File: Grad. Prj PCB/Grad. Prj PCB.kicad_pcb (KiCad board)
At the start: 2 copper layers, 72 x 90 mm, 45 parts, among them J1 GPS, J2 Lock_4, J3 Lock_3, J4 Lock_2, J5 Lock_1, J6 POWER INPUT, J7 Pressure, J8 Heart Rate, J9 Vbatt, K1 POWER RELAY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

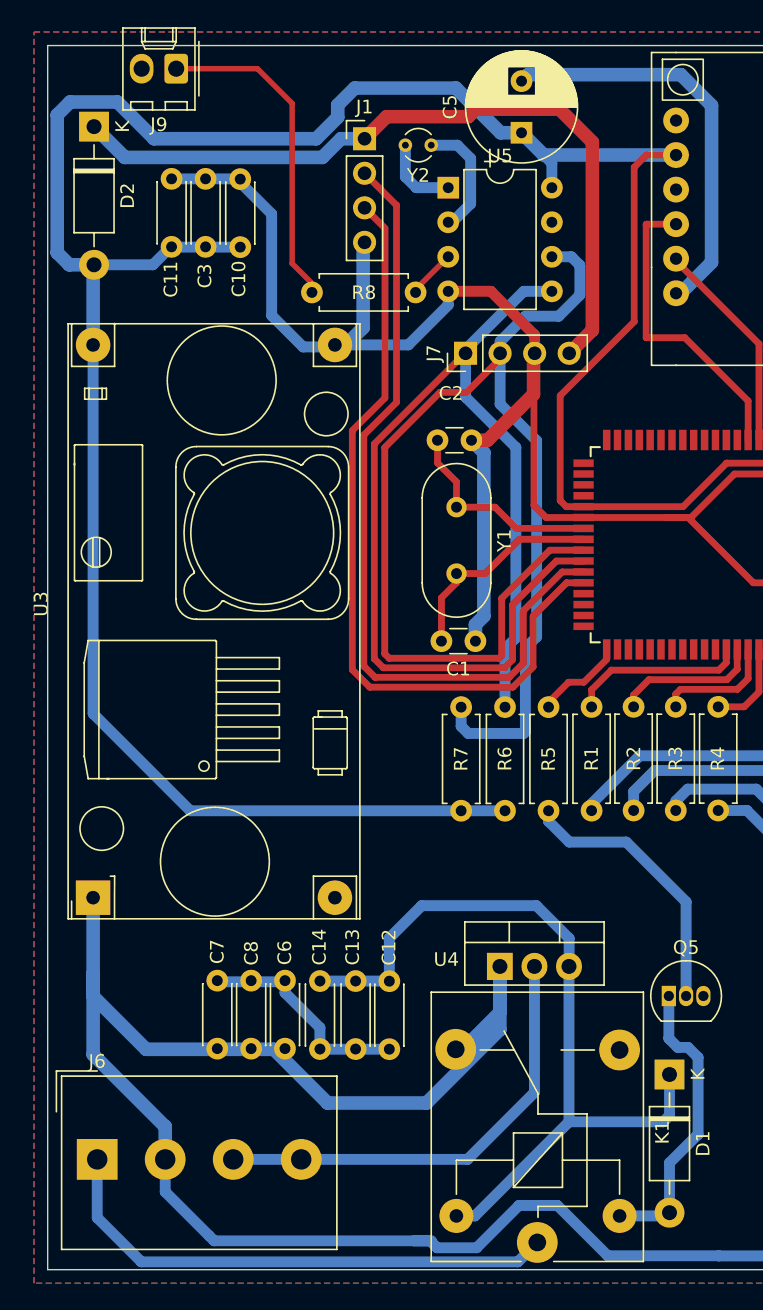
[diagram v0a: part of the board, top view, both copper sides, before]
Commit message: Added RTC
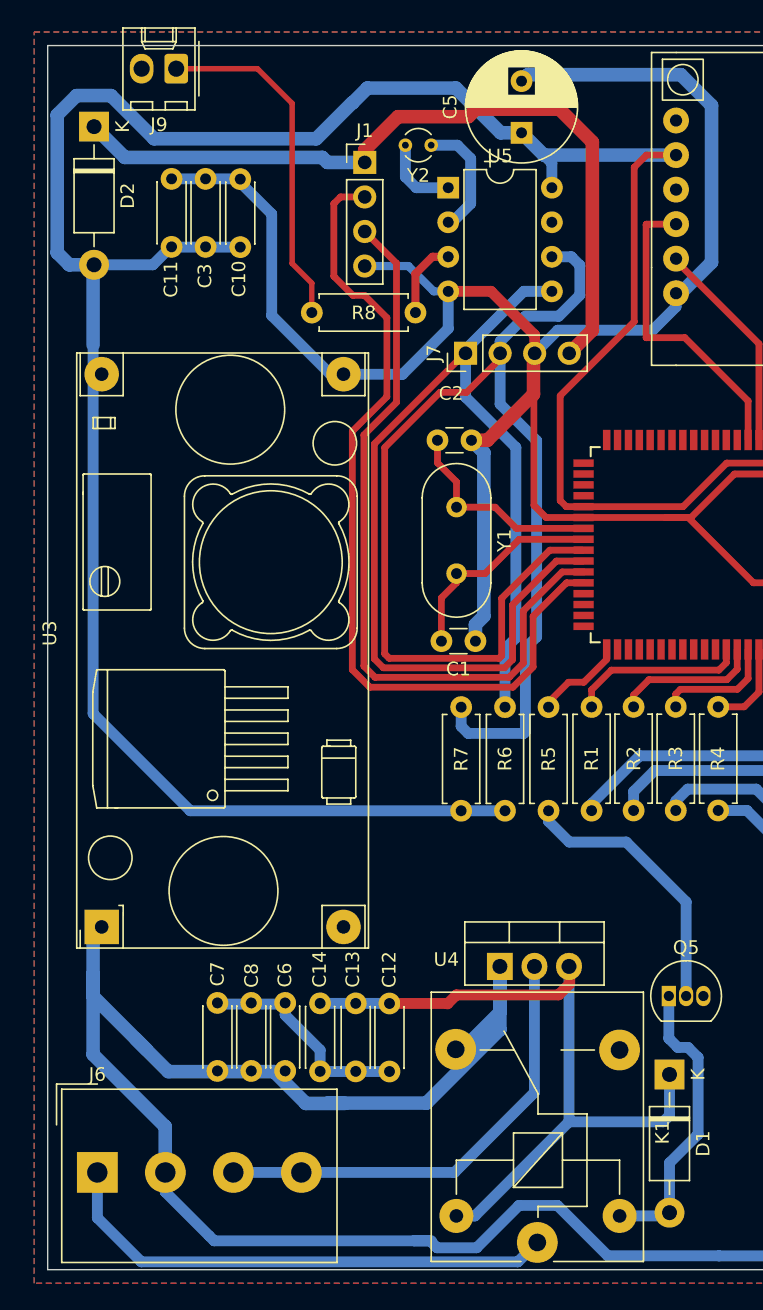
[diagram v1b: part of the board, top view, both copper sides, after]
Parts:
- moved U3 2.24 mm to (74.0, 104.8)
- moved J1 1.74 mm to (93.3, 48.6)
- moved C13 1.64 mm to (92.7, 110.4)
- moved C14 1.64 mm to (90.0, 110.4)
- moved C7 1.64 mm to (82.5, 115.4)
- moved C8 1.64 mm to (85.0, 115.4)
- moved C12 1.64 mm to (95.1, 110.4)
- moved C6 1.64 mm to (87.5, 115.4)
- moved R8 1.48 mm to (97.0, 59.6)
- moved J6 0.96 mm to (73.7, 122.9)
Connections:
- J1 pad 2: TX -> RX
- J1 pad 3: RX -> TX
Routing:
- net GND: track 221.1 -> 235.0 mm
- net +5V: track 58.7 -> 53.5 mm
- net RX: track 58.5 -> 62.8 mm
- net TX: track 60.2 -> 55.9 mm
- net Net-(R8-Pad1): track 4.04 -> 5.78 mm
- net Net-(J9-Pad1): track 24.1 -> 25.6 mm
- net 12vIN: track 38.6 -> 37.6 mm
- net +3.3V: track 56.3 -> 57.1 mm
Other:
- board text added: "+VBatt"
- board text added: "+VLine"
- board text added: "-VBatt"

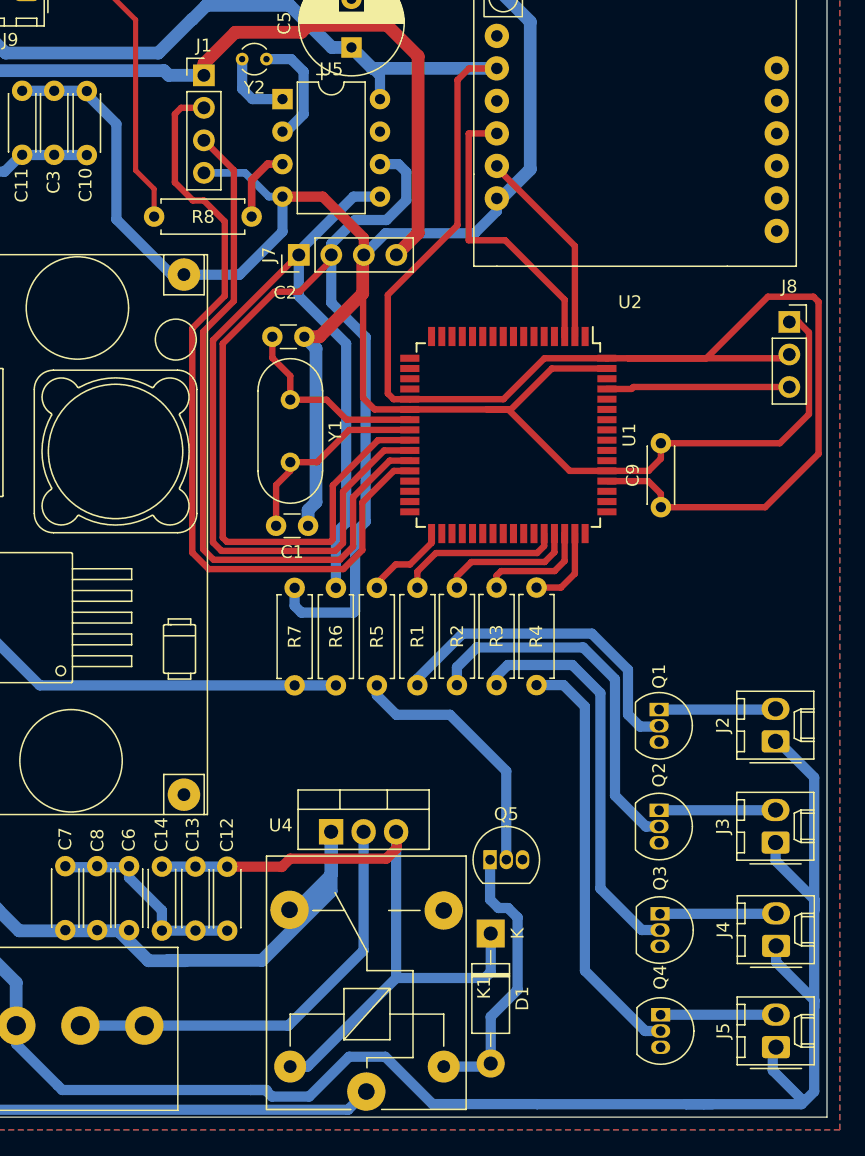
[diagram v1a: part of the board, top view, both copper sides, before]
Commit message: Added ISP Pin Header
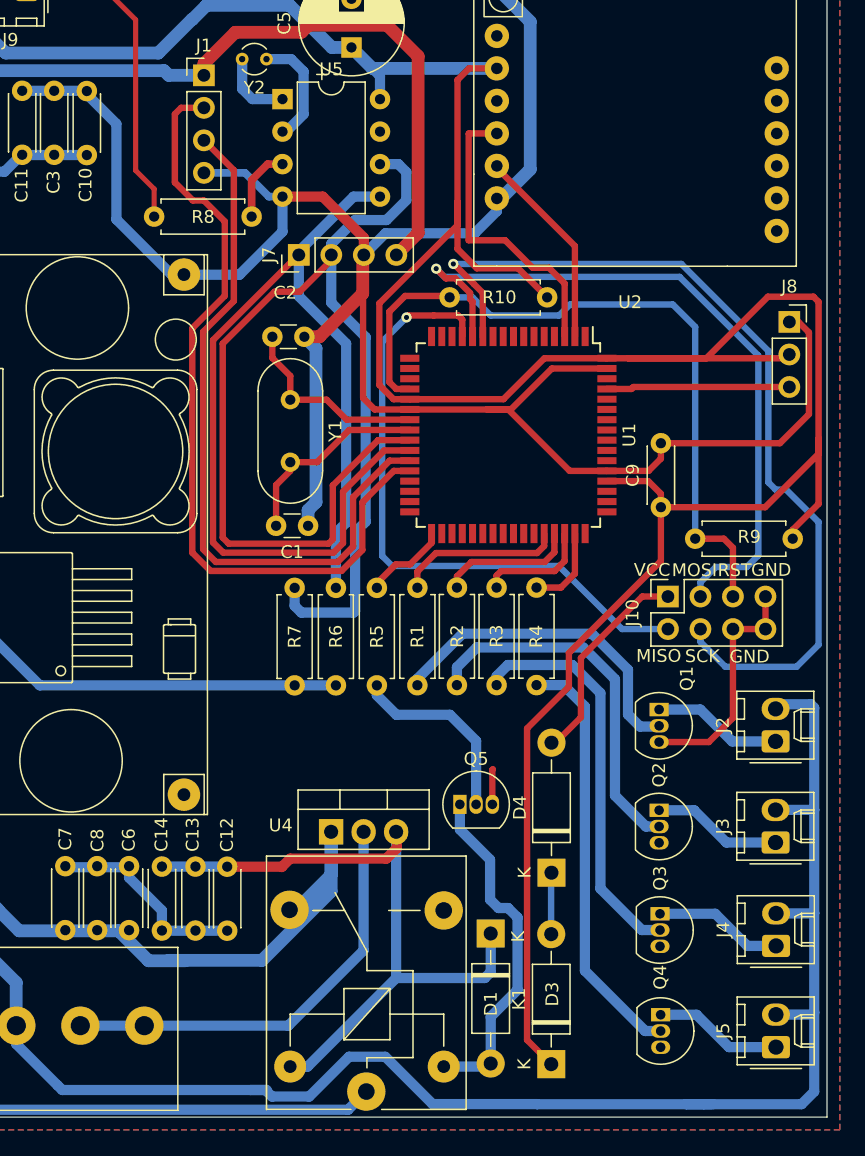
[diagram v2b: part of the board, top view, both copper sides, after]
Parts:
- added D3: 1N4007, Diode_THT:D_DO-41_SOD81_P10.16mm_Horizontal, F.Cu at (120.5, 125.9)
- added D4: 1N4007, Diode_THT:D_DO-41_SOD81_P10.16mm_Horizontal, F.Cu at (120.5, 110.9)
- added J10: ISP, Connector_PinSocket_2.54mm:PinSocket_2x04_P2.54mm_Vertical, F.Cu at (129.6, 89.3)
- added R10: 10K, Resistor_THT:R_Axial_DIN0207_L6.3mm_D2.5mm_P7.62mm_Horizontal, F.Cu at (112.5, 65.9)
- added R9: 10K, Resistor_THT:R_Axial_DIN0207_L6.3mm_D2.5mm_P7.62mm_Horizontal, F.Cu at (139.3, 84.8)
- moved Q5 4.92 mm to (113.3, 105.6)
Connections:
- J2 pad 1: 12vLine -> Lock_4
- J2 pad 2: Lock_4 -> 12vLine
- J3 pad 1: 12vLine -> Lock_3
- J3 pad 2: Lock_3 -> 12vLine
- J4 pad 1: 12vLine -> Lock_2
- J4 pad 2: Lock_2 -> 12vLine
- J5 pad 1: 12vLine -> Lock_1
- J5 pad 2: Lock_1 -> 12vLine
- U1 pad 11: unconnected-(U1-Pad11) -> SCK
- U1 pad 12: unconnected-(U1-Pad12) -> MOSI
- U1 pad 13: unconnected-(U1-Pad13) -> MISO
- U1 pad 20: unconnected-(U1-Pad20) -> RST
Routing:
- net SCK: track 0.00 -> 70.9 mm, vias 0 -> 1
- net +4V: track 258.6 -> 328.6 mm
- net RST: track 0.00 -> 57.1 mm
- net MOSI: track 0.00 -> 57.0 mm, vias 0 -> 1
- net MISO: track 0.00 -> 50.0 mm, vias 0 -> 1
- net GND: track 235.0 -> 256.4 mm
- net Net-(J10-Pad1): track 0.00 -> 16.6 mm
- net Net-(Q5-Pad2): track 20.3 -> 15.0 mm
- net Net-(D1-Pad2): track 21.9 -> 27.2 mm
- net Net-(D3-Pad2): track 0.00 -> 4.82 mm
- net 12vLine: track 191.9 -> 189.0 mm
- net Lock_4: track 9.12 -> 10.3 mm
- net Lock_1: track 9.01 -> 10.1 mm
- net Lock_3: track 9.11 -> 10.1 mm
- net Lock_2: track 9.08 -> 10.1 mm
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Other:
- board text added: "GND"
- board text added: "MISO"
- board text added: "MOSI"
- board text added: "RST"
- board text added: "SCK"
- board text added: "VCC"

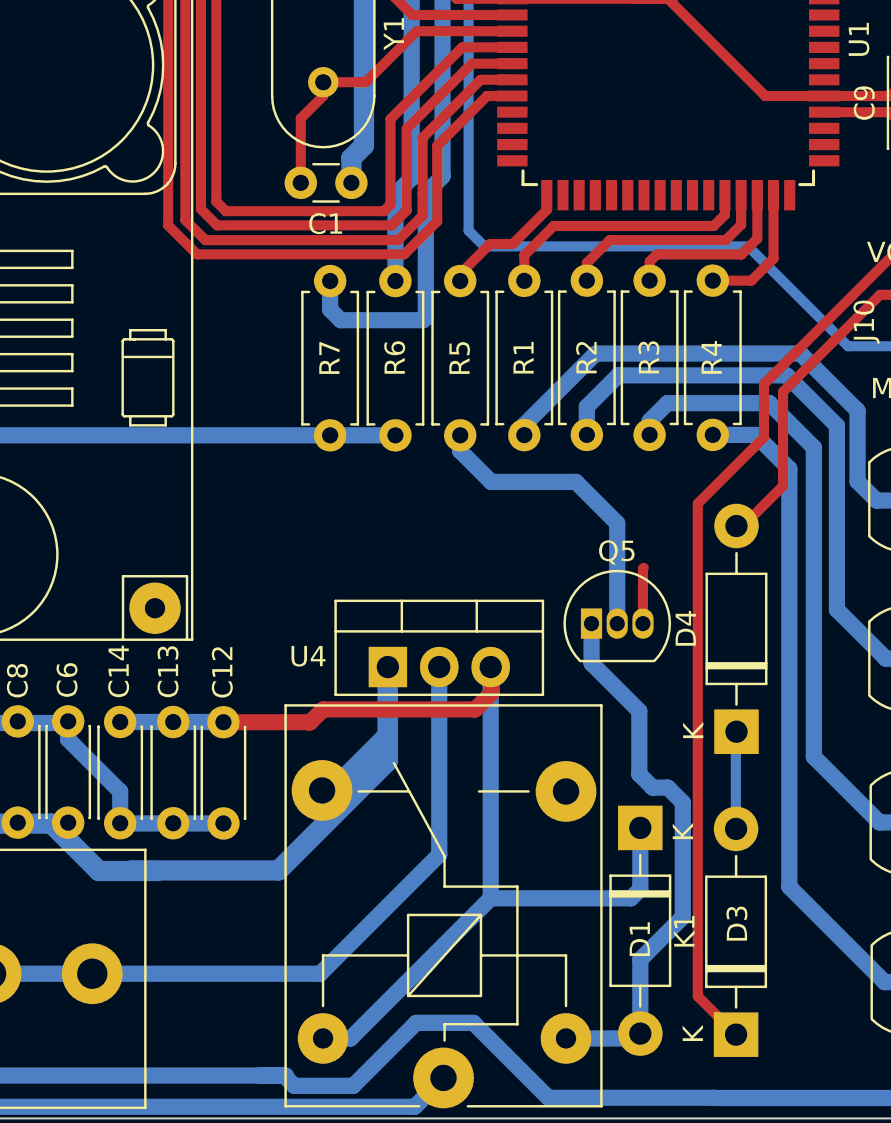
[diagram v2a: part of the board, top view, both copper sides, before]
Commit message: Added ISP Pin Header
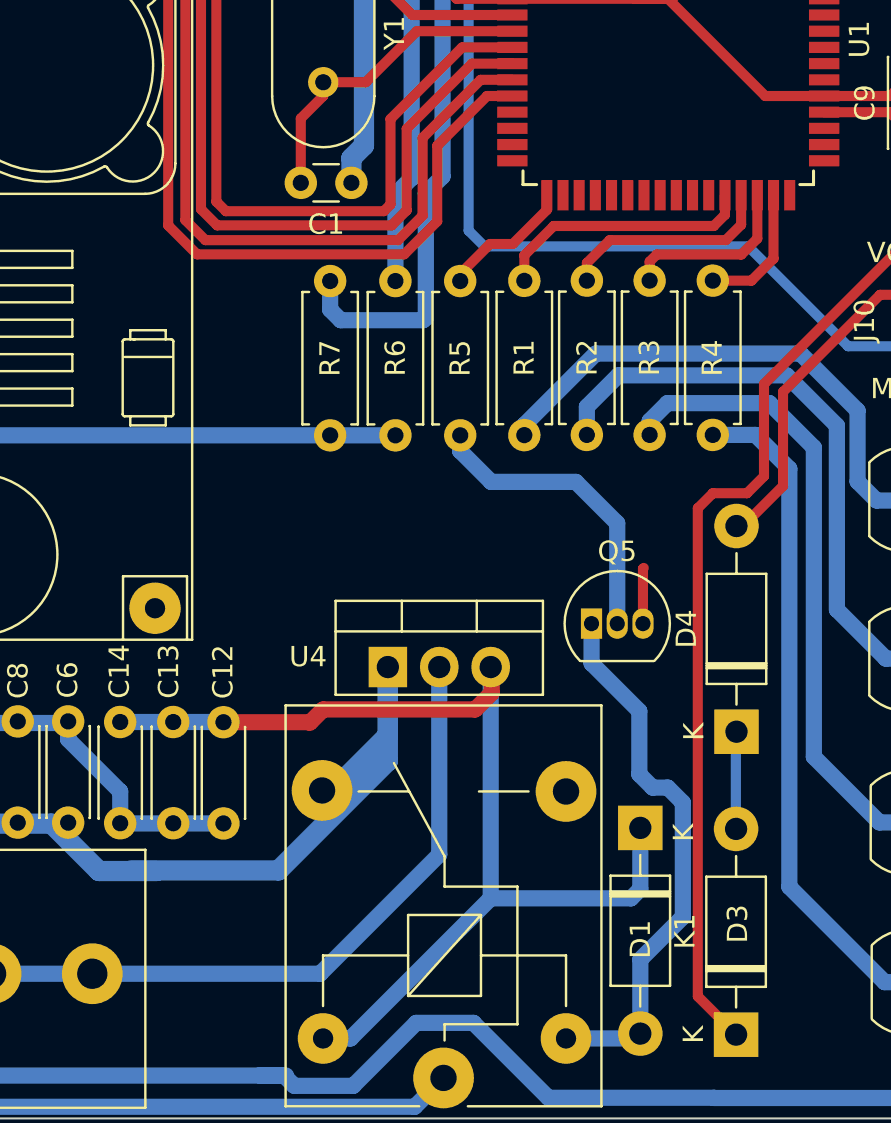
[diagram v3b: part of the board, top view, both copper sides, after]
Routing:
- net +4V: track 328.6 -> 329.6 mm
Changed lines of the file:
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@@
     (fp_arc (start 29.653011 17.437976) (mid 26.817397 18.185797) (end 23.981783 17.437976) (layer "F.SilkS") (width 0.12))
     (fp_arc (start 23.981784 7.433617) (mid 26.817398 6.685796) (end 29.653011 7.433617) (layer "F.SilkS") (width 0.12))
-    (fp_arc (start 23.847611 17.472062) (mid 23.907831 17.428018) (end 23.981783 17.437976) (layer "F.SilkS") (width 0.12))
-    (fp_arc (start 13.181636 16.183217) (mid 13.252317 16.21252) (end 13.281636 16.283217) (layer "F.SilkS") (width 0.12))
+    (fp_arc (start 23.847611 17.472062) (mid 23.907835 17.428062) (end 23.981783 17.437976) (layer "F.SilkS") (width 0.12))
+    (fp_arc (start 13.181636 16.183217) (mid 13.252353 16.212514) (end 13.281636 16.283217) (layer "F.SilkS") (width 0.12))
     (fp_arc (start 21.815217 15.271409) (mid 21.825126 15.345337) (end 21.781132 15.405582) (layer "F.SilkS") (width 0.12))
     (fp_arc (start 23.981783 7.433617) (mid 23.907854 7.443509) (end 23.847611 7.399531) (layer "F.SilkS") (width 0.12))
@@
     (fp_arc (start 31.853663 15.405583) (mid 31.809646 15.345344) (end 31.819576 15.27141) (layer "F.SilkS") (width 0.12))
     (fp_arc (start 33.299783 3.582294) (mid 33.285139 3.617647) (end 33.249783 3.632294) (layer "F.SilkS") (width 0.12))
-    (fp_arc (start 9.581636 18.683217) (mid 9.510896 18.653941) (end 9.481636 18.583217) (layer "F.SilkS") (width 0.12))
+    (fp_arc (start 9.581636 18.683217) (mid 9.510931 18.653935) (end 9.481636 18.583217) (layer "F.SilkS") (width 0.12))
     (fp_arc (start 21.815218 15.27141) (mid 21.067399 12.435797) (end 21.815218 9.600183) (layer "F.SilkS") (width 0.12))
     (fp_arc (start 21.781131 9.46601) (mid 21.825179 9.52623) (end 21.815218 9.600183) (layer "F.SilkS") (width 0.12))
@@
   (segment (start 98.66 69.02) (end 98.66 70.68) (width 0.5) (layer "F.Cu") (net 3))
   (segment (start 104.46 75.5) (end 102.9 73.94) (width 0.5) (layer "F.Cu") (net 3))
-  (segment (start 120.45 125.86) (end 118.56 123.97) (width 0.5) (layer "F.Cu") (net 4))
+  (segment (start 129.02 86.54) (end 129.02 82.34) (width 0.5) (layer "F.Cu") (net 4))
   (segment (start 141.34 82.08) (end 141.34 76.97) (width 0.5) (layer "F.Cu") (net 4))
   (segment (start 138.76 70.7) (end 139.055 70.405) (width 0.5) (layer "F.Cu") (net 4))
@@
   (segment (start 124.8 70.7) (end 126.46 70.7) (width 0.5) (layer "F.Cu") (net 4))
   (segment (start 126.46 70.7) (end 138.76 70.7) (width 0.5) (layer "F.Cu") (net 4))
+  (segment (start 119.3 99.12) (end 120.99 99.12) (width 0.5) (layer "F.Cu") (net 4))
   (segment (start 129.02 82.34) (end 137.17 82.34) (width 0.5) (layer "F.Cu") (net 4))
-  (segment (start 118.56 123.97) (end 118.56 99.63) (width 0.5) (layer "F.Cu") (net 4))
+  (segment (start 121.83 93.73) (end 129.02 86.54) (width 0.5) (layer "F.Cu") (net 4))
+  (segment (start 118.56 123.97) (end 118.56 99.86) (width 0.5) (layer "F.Cu") (net 4))
+  (segment (start 121.83 98.28) (end 121.83 93.73) (width 0.5) (layer "F.Cu") (net 4))
   (segment (start 141.34 76.97) (end 141.34 66.29) (width 0.5) (layer "F.Cu") (net 4))
   (segment (start 109.4 73.9) (end 116.72 73.9) (width 0.5) (layer "F.Cu") (net 4))
@@
   (segment (start 108.13 73.9) (end 107.02 72.79) (width 0.5) (layer "F.Cu") (net 4))
   (segment (start 116.72 73.9) (end 119.92 70.7) (width 0.5) (layer "F.Cu") (net 4))
-  (segment (start 129.02 86.54) (end 129.02 82.34) (width 0.5) (layer "F.Cu") (net 4))
   (segment (start 140.94 65.89) (end 137.38 65.89) (width 0.5) (layer "F.Cu") (net 4))
   (segment (start 129.02 81.29) (end 129.02 82.34) (width 0.5) (layer "F.Cu") (net 4))
@@
   (segment (start 114.64 63.67) (end 113.125 62.155) (width 0.5) (layer "F.Cu") (net 4))
   (segment (start 120.13 65.94) (end 117.86 63.67) (width 0.5) (layer "F.Cu") (net 4))
+  (segment (start 120.45 125.86) (end 118.56 123.97) (width 0.5) (layer "F.Cu") (net 4))
+  (segment (start 118.56 99.86) (end 119.3 99.12) (width 0.5) (layer "F.Cu") (net 4))
   (segment (start 141.34 66.29) (end 140.94 65.89) (width 0.5) (layer "F.Cu") (net 4))
   (segment (start 141.34 78.17) (end 141.34 76.97) (width 0.5) (layer "F.Cu") (net 4))
   (segment (start 107.02 66.41) (end 113.125 60.305) (width 0.5) (layer "F.Cu") (net 4))
-  (segment (start 118.56 99.63) (end 121.83 96.36) (width 0.5) (layer "F.Cu") (net 4))
-  (segment (start 121.83 96.36) (end 121.83 93.73) (width 0.5) (layer "F.Cu") (net 4))
   (segment (start 113.125 60.305) (end 113.125 58.495) (width 0.5) (layer "F.Cu") (net 4))
   (segment (start 139.32 84.1) (end 141.34 82.08) (width 0.5) (layer "F.Cu") (net 4))
+  (segment (start 120.99 99.12) (end 121.83 98.28) (width 0.5) (layer "F.Cu") (net 4))
   (segment (start 114.03 48.05) (end 116.2 48.05) (width 0.5) (layer "F.Cu") (net 4))
   (segment (start 124.8 80.3) (end 128.03 80.3) (width 0.5) (layer "F.Cu") (net 4))
   (segment (start 113.125 48.955) (end 114.03 48.05) (width 0.5) (layer "F.Cu") (net 4))
-  (segment (start 121.83 93.73) (end 129.02 86.54) (width 0.5) (layer "F.Cu") (net 4))
   (segment (start 119.92 70.7) (end 124.8 70.7) (width 0.5) (layer "F.Cu") (net 4))
   (segment (start 113.125 62.155) (end 113.125 58.495) (width 0.5) (layer "F.Cu") (net 4))
